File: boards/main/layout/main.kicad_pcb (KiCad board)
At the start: 4 copper layers, 150 parts, among them IC1 STM32H725RGV6, IC2 LSM6DSVTR, IC3 TSC2020IYST, IC4 TSC2020IYST, IC5 L6205D013TR, IC6 STSPIN958TR, IC7 L6981N33DR, J1 B02B-PASK(LF)(SN), M1 B02B-PASK(LF)(SN), M2 B02B-PASK(LF)(SN), M3 B02B-PASK(LF)(SN), P1 PZ254V-11-04P, Q1 AO3400A, Q2 AO3400A, Q3 AO3400A, Q4 AO3400A, Q5 AO3400A, Q6 HSBB3072, SW1 DSHP04TJGER, SW2 GT-TC048B-H025-L1, SW3 GT-TC048B-H025-L1, SW4 MK-12D18-G040, SW5 GT-TC048B-H025-L1, U1 TPS611781RNWR, U2 GT-USB-7010ASV, U3 CJA1117B-3.3

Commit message: ✨ Add the M2 screw holes to the main board
The previous board's four screw holes were footprints without a designator. They are now
H1-H4, instances of a new micras/MountingHole package (2.4 mm NPTH, the previous footprint),
declared in changes.toml as added parts.
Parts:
- added H1: MountingHole, Team-Micras_MicrasPCB_components_micras_MountingHole:MountingHole_2.4mm_NPTH, F.Cu at (193.6, 118.4)
- added H2: MountingHole, Team-Micras_MicrasPCB_components_micras_MountingHole:MountingHole_2.4mm_NPTH, F.Cu at (193.6, 116.0)
- added H3: MountingHole, Team-Micras_MicrasPCB_components_micras_MountingHole:MountingHole_2.4mm_NPTH, F.Cu at (193.6, 113.6)
- added H4: MountingHole, Team-Micras_MicrasPCB_components_micras_MountingHole:MountingHole_2.4mm_NPTH, F.Cu at (193.6, 111.2)

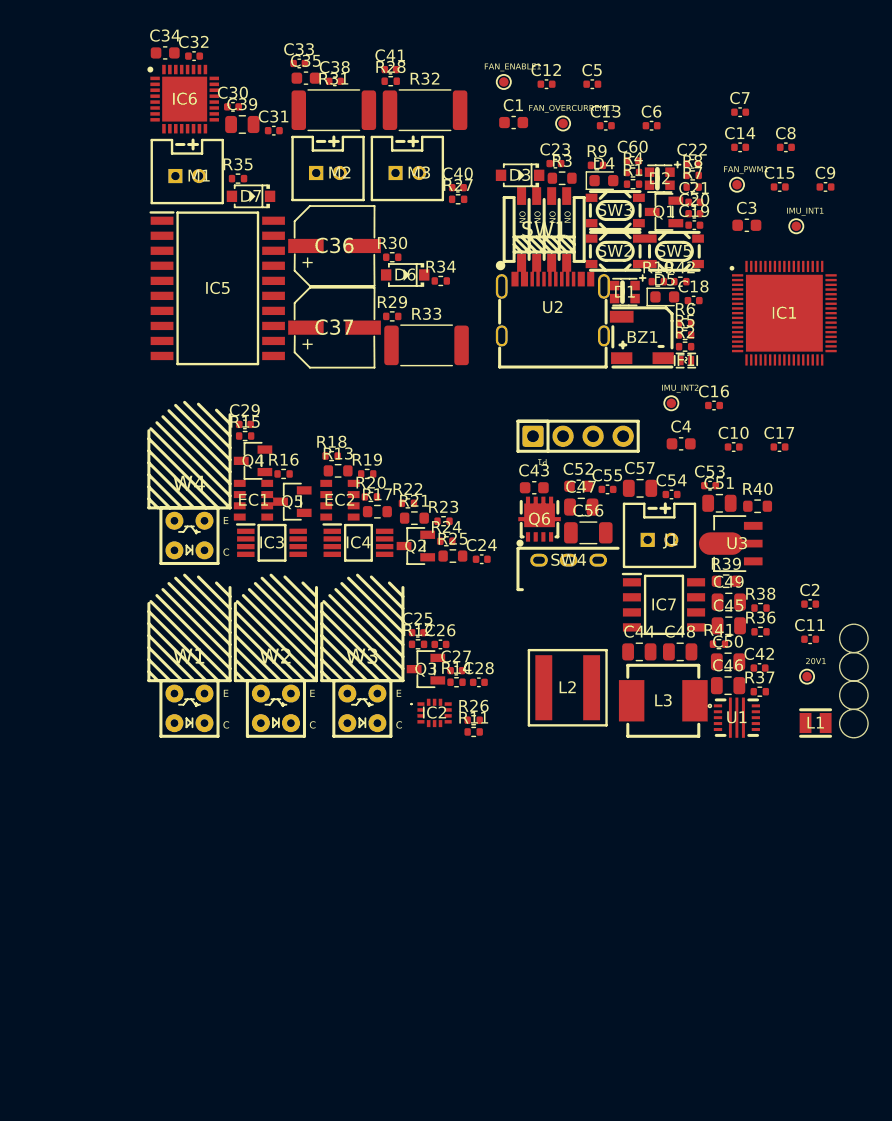
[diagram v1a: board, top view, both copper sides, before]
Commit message: 🚚 Transfer the previous main board's placement, routing and outline
boards/main/previous/transfer_layout.py copies the previous revision's copper, zones and board
graphics with each net renamed by pad membership, places every footprint by designator (stdlib
generic R/C/LED footprints fitted onto the old pads), keeps the old reference text and the aux and
grid origins, refills the zones and syncs with pcb layout. Teardrop zones become plain zones with
stable UUIDs: KiCad 10 does not save teardrop UUIDs, so a board with teardrops is never
byte-stable.

boards/main/previous/rework.py makes the two copper changes: C1 (IC1 pin 1, C8 and C9 off the
battery chain, onto 3V3 with a bridge to pin 68) and C2 (VFBSMPS and VCAP1-3 joined on an
In2.Cu VCORE route).
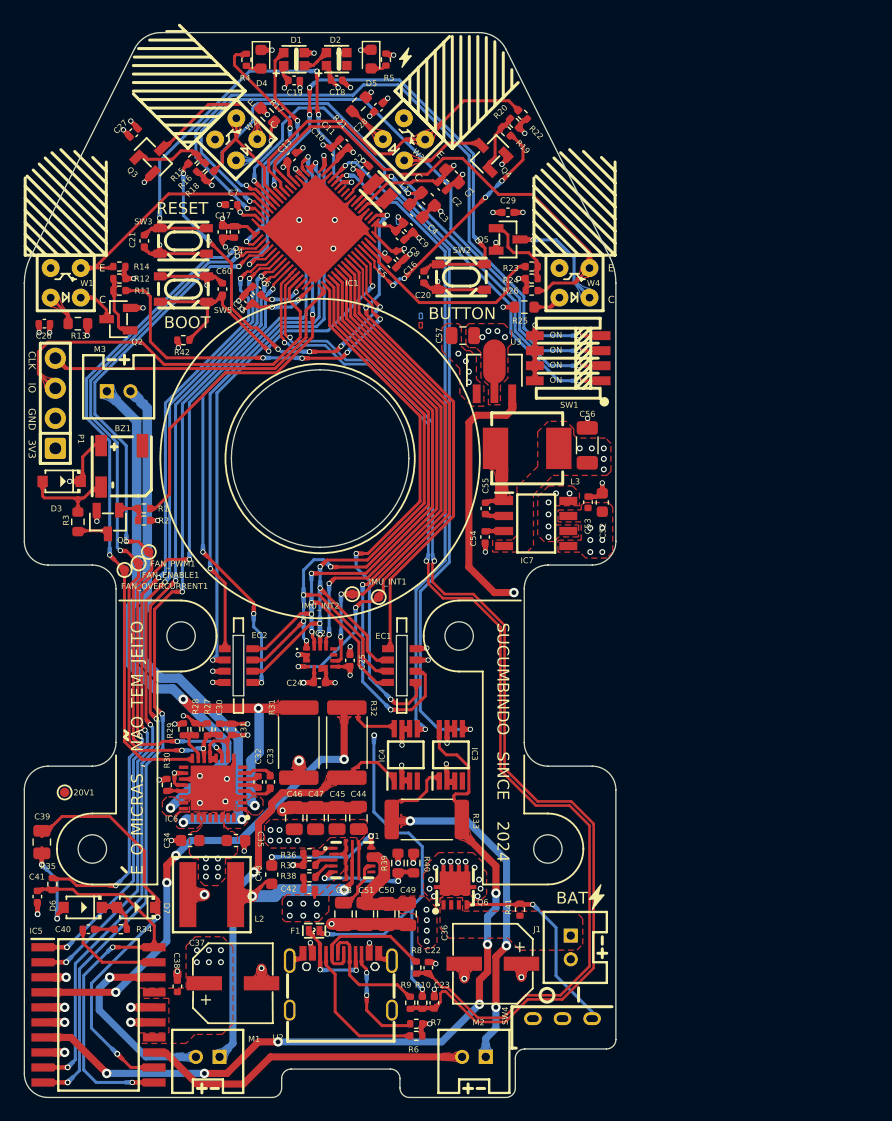
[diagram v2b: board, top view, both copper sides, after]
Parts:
- moved C38 77.6 mm to (136.4, 140.6), turned to -90 degrees
- moved C41 76.0 mm to (124.6, 133.0), turned to -90 degrees
- moved M2 75.4 mm to (160.5, 146.6), turned to 180 degrees
- moved R7 74.5 mm to (156.6, 143.8), turned to 180 degrees
- moved M1 74.4 mm to (138.0, 146.6), turned to 180 degrees
- moved R9 72.5 mm to (156.1, 142.0), turned to -90 degrees
- moved C23 71.7 mm to (158.2, 142.0), turned to -90 degrees
- moved C22 71.5 mm to (157.6, 139.0), turned to -90 degrees
- moved R8 70.9 mm to (156.6, 139.0), turned to -90 degrees
- moved C40 70.0 mm to (128.9, 135.8), turned to 180 degrees
- moved C34 66.6 mm to (137.5, 128.3), turned to 180 degrees
- moved H3 66.2 mm to (129.3, 129.0)
- moved C35 64.7 mm to (141.4, 128.3)
- moved R6 64.4 mm to (156.6, 144.8), turned to 180 degrees
- moved R10 64.1 mm to (157.1, 142.0), turned to 90 degrees
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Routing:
- net GND: track 0.00 -> 147.6 mm, vias 0 -> 103
- net 3V3: track 0.00 -> 116.7 mm, vias 0 -> 44
- net USBD_P: track 0.00 -> 95.7 mm, vias 0 -> 2
- net USBD_N: track 0.00 -> 94.4 mm, vias 0 -> 2
- net Motor_Right_PWM_BW: track 0.00 -> 80.1 mm, vias 0 -> 4
- net Motor_Right_PWM_FW: track 0.00 -> 78.6 mm, vias 0 -> 4
- net Motor_Left_PWM_BW: track 0.00 -> 70.1 mm, vias 0 -> 4
- net Motor_Left_PWM_FW: track 0.00 -> 69.4 mm, vias 0 -> 4
- net Motor_L_Sense+: track 0.00 -> 68.7 mm, vias 0 -> 6
- net Motor_Enable: track 0.00 -> 65.2 mm, vias 0 -> 4
- net Fan_Enable: track 0.00 -> 62.2 mm, vias 0 -> 4
- net DRIVERS.FAN_LSS: track 0.00 -> 62.0 mm, vias 0 -> 4
- net Fan_PWM: track 0.00 -> 61.4 mm, vias 0 -> 4
- net Switch_3: track 0.00 -> 60.4 mm, vias 0 -> 2
- net SPI_MISO: track 0.00 -> 59.5 mm, vias 0 -> 4
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- added copper zone on B.Cu, net +20V
- added copper zone on F.Cu, net +20V
- added copper zone on In2.Cu, net +20V
- added copper zone on F.Cu, net +5V
- added copper zone on In2.Cu, net +5V
- added copper zone on B.Cu, net 3V3
- added copper zone on F.Cu, net 3V3
- added copper zone on In2.Cu, net 3V3
- added copper zone on B.Cu, net Boot
- added copper zone on F.Cu, net Boot
- added copper zone on B.Cu, net Button
- added copper zone on F.Cu, net Button
- added copper zone on B.Cu, net Buzzer
- added copper zone on F.Cu, net Buzzer
- added copper zone on B.Cu, net Current_Sensor_Left
- added copper zone on F.Cu, net Current_Sensor_Left
- added copper zone on B.Cu, net Current_Sensor_Right
- added copper zone on F.Cu, net Current_Sensor_Right
- added copper zone on B.Cu, net DRIVERS.BRIDGE_EN
- added copper zone on F.Cu, net DRIVERS.BRIDGE_EN
- added copper zone on B.Cu, net DRIVERS.BRIDGE_OUT2A
- added copper zone on F.Cu, net DRIVERS.BRIDGE_OUT2A
- added copper zone on F.Cu, net DRIVERS.BRIDGE_OUT2B
- added copper zone on F.Cu, net DRIVERS.BRIDGE_PUMP
- added copper zone on F.Cu, net DRIVERS.BRIDGE_PUMP_RC
- added copper zone on B.Cu, net DRIVERS.BRIDGE_VBOOT
- added copper zone on F.Cu, net DRIVERS.BRIDGE_VBOOT
- added copper zone on F.Cu, net DRIVERS.BRIDGE_VCP
- added copper zone on F.Cu, net DRIVERS.FAN_CP1
- added copper zone on F.Cu, net DRIVERS.FAN_CP2
- added copper zone on B.Cu, net DRIVERS.FAN_LSS
- added copper zone on F.Cu, net DRIVERS.FAN_LSS
- added copper zone on B.Cu, net DRIVERS.FAN_OUT
- added copper zone on F.Cu, net DRIVERS.FAN_OUT
- added copper zone on F.Cu, net DRIVERS.FAN_REF
- added copper zone on F.Cu, net DRIVERS.FAN_SR
- added copper zone on F.Cu, net DRIVERS.FAN_VBOOT
- added copper zone on F.Cu, net DRIVERS.FAN_VSPUMP
- added copper zone on B.Cu, net Encoder_Left_ABI_A
- added copper zone on F.Cu, net Encoder_Left_ABI_A
- added copper zone on B.Cu, net Encoder_Left_ABI_B
- added copper zone on F.Cu, net Encoder_Left_ABI_B
- added copper zone on B.Cu, net Encoder_Left_CSn
- added copper zone on F.Cu, net Encoder_Left_CSn
- added copper zone on B.Cu, net Encoder_Right_ABI_A
- added copper zone on F.Cu, net Encoder_Right_ABI_A
- added copper zone on B.Cu, net Encoder_Right_ABI_B
- added copper zone on F.Cu, net Encoder_Right_ABI_B
- added copper zone on B.Cu, net Encoder_Right_CSn
- added copper zone on F.Cu, net Encoder_Right_CSn
- added copper zone on B.Cu, net Fan_Enable
- added copper zone on F.Cu, net Fan_Enable
- added copper zone on B.Cu, net Fan_Overcurrent
- added copper zone on F.Cu, net Fan_Overcurrent
- added copper zone on B.Cu, net Fan_PWM
- added copper zone on F.Cu, net Fan_PWM
- added copper zone on F.Cu, net GND
- added copper zone on In1.Cu, net GND
- added copper zone on F.Cu, net GND_BAT
- added copper zone on B.Cu, net IMU_INT1
- added copper zone on F.Cu, net IMU_INT1
- added copper zone on B.Cu, net IMU_INT2
- added copper zone on F.Cu, net IMU_INT2
- added copper zone on B.Cu, net IMU_SPI_CSn
- added copper zone on F.Cu, net IMU_SPI_CSn
- added copper zone on B.Cu, net LED_ARGB
- added copper zone on F.Cu, net LED_ARGB
- added copper zone on B.Cu, net LED_Blue
- added copper zone on F.Cu, net LED_Blue
- added copper zone on B.Cu, net Motor_Enable
- added copper zone on F.Cu, net Motor_Enable
- added copper zone on F.Cu, net Motor_L_Sense+
- added copper zone on B.Cu, net Motor_L_Sense-
- added copper zone on F.Cu, net Motor_L_Sense-
- added copper zone on B.Cu, net Motor_Left_PWM_BW
- added copper zone on F.Cu, net Motor_Left_PWM_BW
- added copper zone on B.Cu, net Motor_Left_PWM_FW
- added copper zone on F.Cu, net Motor_Left_PWM_FW
- added copper zone on F.Cu, net Motor_R_Sense+
- added copper zone on B.Cu, net Motor_R_Sense-
- added copper zone on F.Cu, net Motor_R_Sense-
- added copper zone on B.Cu, net Motor_Right_PWM_BW
- added copper zone on F.Cu, net Motor_Right_PWM_BW
- added copper zone on B.Cu, net Motor_Right_PWM_FW
- added copper zone on F.Cu, net Motor_Right_PWM_FW
- added copper zone on F.Cu, net PERIPHERALS.BUZZER_COIL
- added copper zone on F.Cu, net PERIPHERALS.BUZZER_DRAIN
- added copper zone on F.Cu, net PERIPHERALS.BUZZER_GATE
- added copper zone on F.Cu, net PERIPHERALS.LED_CHAIN
- added copper zone on F.Cu, net PERIPHERALS.LED_RED_A
- added copper zone on F.Cu, net PERIPHERALS.LED_YELLOW_A
- added copper zone on B.Cu, net PERIPHERALS.SBU_PWR
- added copper zone on F.Cu, net PERIPHERALS.SBU_PWR
- added copper zone on F.Cu, net PERIPHERALS.USB_CC1
- added copper zone on B.Cu, net PERIPHERALS.USB_CC2
- added copper zone on F.Cu, net PERIPHERALS.USB_CC2
- added copper zone on F.Cu, net PERIPHERALS.USB_CONN_D_N
- added copper zone on F.Cu, net PERIPHERALS.USB_CONN_D_P
- added copper zone on B.Cu, net REGULATORS.BAT_SW_GATE
- added copper zone on F.Cu, net REGULATORS.BAT_SW_GATE
- added copper zone on B.Cu, net REGULATORS.BOOST_BST
- added copper zone on F.Cu, net REGULATORS.BOOST_BST
- added copper zone on F.Cu, net REGULATORS.BOOST_COMP
- added copper zone on F.Cu, net REGULATORS.BOOST_COMP_RC
- added copper zone on B.Cu, net REGULATORS.BOOST_FB
- added copper zone on F.Cu, net REGULATORS.BOOST_FB
- added copper zone on F.Cu, net REGULATORS.BOOST_FREQ
- added copper zone on F.Cu, net REGULATORS.BOOST_ILIM
- added copper zone on F.Cu, net REGULATORS.BOOST_SW
- added copper zone on F.Cu, net REGULATORS.BOOST_VCC
- added copper zone on F.Cu, net REGULATORS.BUCK_BOOT
- added copper zone on F.Cu, net REGULATORS.BUCK_SW
- added copper zone on F.Cu, net REGULATORS.BUCK_VCC
- added copper zone on B.Cu, net Reset
- added copper zone on F.Cu, net Reset
- added copper zone on F.Cu, net SENSORS.WALL0_GATE
- added copper zone on F.Cu, net SENSORS.WALL0_LED_A
- added copper zone on F.Cu, net SENSORS.WALL0_LED_K
- added copper zone on F.Cu, net SENSORS.WALL1_GATE
- added copper zone on B.Cu, net SENSORS.WALL1_LED_A
- added copper zone on F.Cu, net SENSORS.WALL1_LED_A
- added copper zone on F.Cu, net SENSORS.WALL1_LED_K
- added copper zone on F.Cu, net SENSORS.WALL2_GATE
- added copper zone on F.Cu, net SENSORS.WALL2_LED_A
- added copper zone on F.Cu, net SENSORS.WALL2_LED_K
- added copper zone on F.Cu, net SENSORS.WALL3_GATE
- added copper zone on F.Cu, net SENSORS.WALL3_LED_A
- added copper zone on B.Cu, net SENSORS.WALL3_LED_K
- added copper zone on F.Cu, net SENSORS.WALL3_LED_K
- added copper zone on F.Cu, net SMPS_LX
- added copper zone on B.Cu, net SPI_MISO
- added copper zone on F.Cu, net SPI_MISO
- added copper zone on B.Cu, net SPI_MOSI
- added copper zone on F.Cu, net SPI_MOSI
- added copper zone on B.Cu, net SPI_SCK
- added copper zone on F.Cu, net SPI_SCK
- added copper zone on F.Cu, net SWCLK
- added copper zone on F.Cu, net SWDIO
- added copper zone on B.Cu, net Switch_0
- added copper zone on F.Cu, net Switch_0
- added copper zone on B.Cu, net Switch_1
- added copper zone on F.Cu, net Switch_1
- added copper zone on B.Cu, net Switch_2
- added copper zone on F.Cu, net Switch_2
- added copper zone on B.Cu, net Switch_3
- added copper zone on F.Cu, net Switch_3
- added copper zone on B.Cu, net USBD_N
- added copper zone on F.Cu, net USBD_N
- added copper zone on B.Cu, net USBD_P
- added copper zone on F.Cu, net USBD_P
- added copper zone on B.Cu, net VBAT
- added copper zone on F.Cu, net VBAT
- added copper zone on In2.Cu, net VBAT
- added copper zone on B.Cu, net VCORE
- added copper zone on F.Cu, net VCORE
- added copper zone on F.Cu, net Wall_Sensor_0
- added copper zone on F.Cu, net Wall_Sensor_1
- added copper zone on F.Cu, net Wall_Sensor_2
- added copper zone on F.Cu, net Wall_Sensor_3
- added copper zone on B.Cu, net Wall_Sensor_PWM_0
- added copper zone on F.Cu, net Wall_Sensor_PWM_0
- added copper zone on B.Cu, net Wall_Sensor_PWM_1
- added copper zone on F.Cu, net Wall_Sensor_PWM_1
- added copper zone on B.Cu, net Wall_Sensor_PWM_2
- added copper zone on F.Cu, net Wall_Sensor_PWM_2
- added copper zone on F.Cu, net Wall_Sensor_PWM_3
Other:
- board outline added: 50 x 90 mm
- board text added: ","
- board text added: "2024"
- board text added: "3V3"
- board text added: "BAT"
- board text added: "BOOT"
- board text added: "BUTTON"
- board text added: "CLK"
- board text added: "E"
- board text added: "GND"
- board text added: "IO"
- board text added: "JEITO"
- board text added: "MICRAS"
- board text added: "NAO"
- board text added: "O"
- board text added: "OFF"
- board text added: "ON"
- board text added: "RESET"
- board text added: "SINCE"
- board text added: "SUCUMBINDO"
- board text added: "TEM"
